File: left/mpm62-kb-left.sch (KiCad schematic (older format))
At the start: 65 parts, among them J1 Conn_01x04_Male, SW1 SW_Push, U1 ProMicro

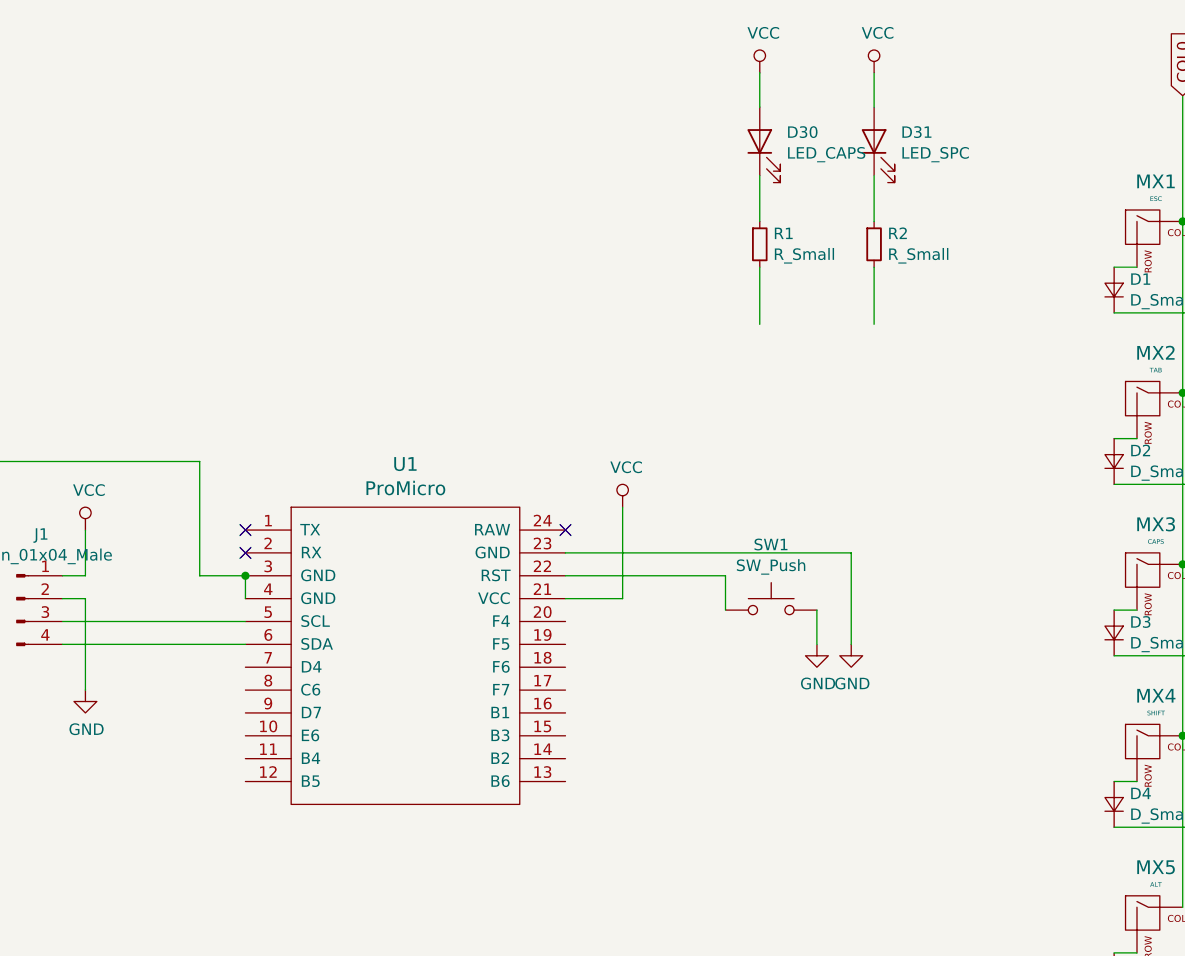
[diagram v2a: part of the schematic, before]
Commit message: Left side routed.
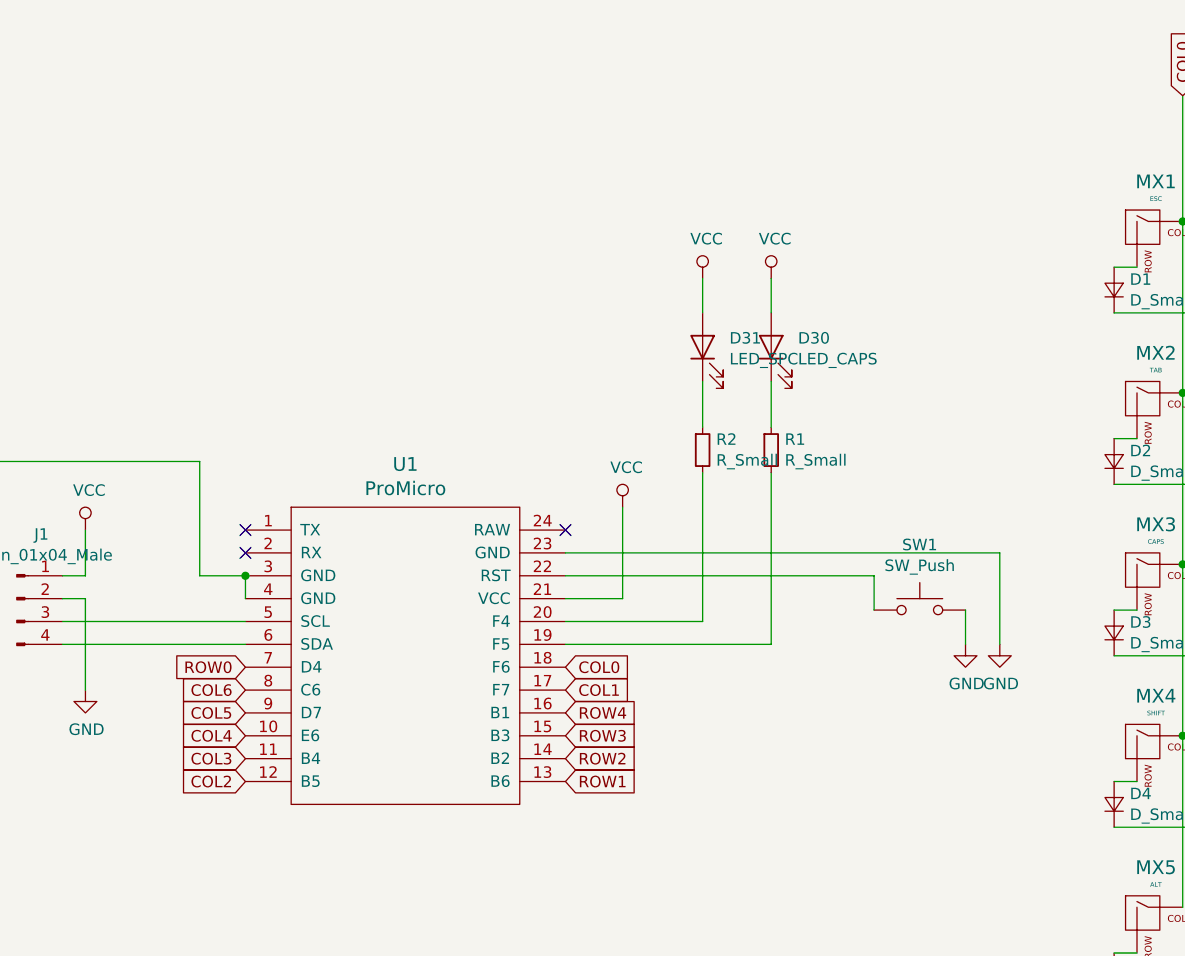
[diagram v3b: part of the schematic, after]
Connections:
- net COL0: now also U1.18 (F6)
- net COL1: now also U1.17 (F7)
- net COL2: now also U1.12 (B5)
- net COL3: now also U1.11 (B4)
- net COL4: now also U1.10 (E6)
- net COL5: now also U1.9 (D7)
- net COL6: now also U1.8 (C6)
- net ROW0: now also U1.7 (D4)
- net ROW1: now also U1.13 (B6)
- net ROW2: now also U1.14 (B2)
- net ROW3: now also U1.15 (B3)
- net ROW4: now also U1.16 (B1)
- net at U1.19 (F5): now also R1.2
- net at U1.20 (F4): now also R2.2
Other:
- moved on the sheet: D30, D31, R1, R2, SW1
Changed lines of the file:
@@
 L Device:R_Small R1
 U 1 1 5F89BC79
-P 4800 2150
-F 0 "R1" H 4859 2196 50  0000 L CNN
-F 1 "R_Small" H 4859 2105 50  0000 L CNN
-F 2 "Resistor_THT:R_Axial_DIN0204_L3.6mm_D1.6mm_P5.08mm_Horizontal" H 4800 2150 50  0001 C CNN
-F 3 "~" H 4800 2150 50  0001 C CNN
-	1    4800 2150
-	1    0    0    -1
-$EndComp
-Wire Wire Line
-	4800 1400 4800 1550
+P 4850 3050
+F 0 "R1" H 4909 3096 50  0000 L CNN
+F 1 "R_Small" H 4909 3005 50  0000 L CNN
+F 2 "Resistor_THT:R_Axial_DIN0204_L3.6mm_D1.6mm_P5.08mm_Horizontal" H 4850 3050 50  0001 C CNN
+F 3 "~" H 4850 3050 50  0001 C CNN
+	1    4850 3050
+	1    0    0    -1
+$EndComp
+Wire Wire Line
+	4850 2300 4850 2450
 $Comp
 L Device:LED D30
 U 1 1 5F893C40
-P 4800 1700
-F 0 "D30" V 4839 1583 50  0000 R CNN
-F 1 "LED_CAPS" V 4748 1583 50  0000 R CNN
-F 2 "LED_THT:LED_D3.0mm" H 4800 1700 50  0001 C CNN
-F 3 "~" H 4800 1700 50  0001 C CNN
-	1    4800 1700
+P 4850 2600
+F 0 "D30" V 4889 2483 50  0000 R CNN
+F 1 "LED_CAPS" V 4798 2483 50  0000 R CNN
+F 2 "LED_THT:LED_D3.0mm" H 4850 2600 50  0001 C CNN
+F 3 "~" H 4850 2600 50  0001 C CNN
+	1    4850 2600
 	0    -1   -1   0
 $EndComp
 Wire Wire Line
-	4800 1850 4800 2050
-Wire Wire Line
-	4800 2250 4800 2500
+	4850 2750 4850 2950
 $Comp
 L Device:R_Small R2
 U 1 1 5F8B9477
-P 5300 2150
-F 0 "R2" H 5359 2196 50  0000 L CNN
-F 1 "R_Small" H 5359 2105 50  0000 L CNN
-F 2 "Resistor_THT:R_Axial_DIN0204_L3.6mm_D1.6mm_P5.08mm_Horizontal" H 5300 2150 50  0001 C CNN
-F 3 "~" H 5300 2150 50  0001 C CNN
-	1    5300 2150
-	1    0    0    -1
-$EndComp
-Wire Wire Line
-	5300 1400 5300 1550
+P 4550 3050
+F 0 "R2" H 4609 3096 50  0000 L CNN
+F 1 "R_Small" H 4609 3005 50  0000 L CNN
+F 2 "Resistor_THT:R_Axial_DIN0204_L3.6mm_D1.6mm_P5.08mm_Horizontal" H 4550 3050 50  0001 C CNN
+F 3 "~" H 4550 3050 50  0001 C CNN
+	1    4550 3050
+	1    0    0    -1
+$EndComp
+Wire Wire Line
+	4550 2300 4550 2450
 $Comp
 L Device:LED D31
 U 1 1 5F8B947E
-P 5300 1700
-F 0 "D31" V 5339 1583 50  0000 R CNN
-F 1 "LED_SPC " V 5248 1583 50  0000 R CNN
-F 2 "LED_THT:LED_D3.0mm" H 5300 1700 50  0001 C CNN
-F 3 "~" H 5300 1700 50  0001 C CNN
-	1    5300 1700
+P 4550 2600
+F 0 "D31" V 4589 2483 50  0000 R CNN
+F 1 "LED_SPC " V 4498 2483 50  0000 R CNN
+F 2 "LED_THT:LED_D3.0mm" H 4550 2600 50  0001 C CNN
+F 3 "~" H 4550 2600 50  0001 C CNN
+	1    4550 2600
 	0    -1   -1   0
 $EndComp
 Wire Wire Line
-	5300 1850 5300 2050
-Wire Wire Line
-	5300 2250 5300 2500
+	4550 2750 4550 2950
 $Comp
 L promicro:ProMicro U1
@@
 L power:GND #PWR0102
 U 1 1 5F790069
-P 5200 3900
-F 0 "#PWR0102" H 5200 3650 50  0001 C CNN
-F 1 "GND" H 5205 3727 50  0000 C CNN
-F 2 "" H 5200 3900 50  0001 C CNN
-F 3 "" H 5200 3900 50  0001 C CNN
-	1    5200 3900
-	1    0    0    -1
-$EndComp
-Wire Wire Line
-	5200 3500 3950 3500
+P 5850 3900
+F 0 "#PWR0102" H 5850 3650 50  0001 C CNN
+F 1 "GND" H 5855 3727 50  0000 C CNN
+F 2 "" H 5850 3900 50  0001 C CNN
+F 3 "" H 5850 3900 50  0001 C CNN
+	1    5850 3900
+	1    0    0    -1
+$EndComp
 $Comp
 L Switch:SW_Push SW1
 U 1 1 5F7953DA
-P 4850 3750
-F 0 "SW1" H 4850 4035 50  0000 C CNN
-F 1 "SW_Push" H 4850 3944 50  0000 C CNN
-F 2 "random-keyboard-parts:SKQG-1155865" H 4850 3950 50  0001 C CNN
-F 3 "~" H 4850 3950 50  0001 C CNN
-	1    4850 3750
-	1    0    0    -1
-$EndComp
-Wire Wire Line
-	3950 3600 4650 3600
-Wire Wire Line
-	4650 3600 4650 3750
+P 5500 3750
+F 0 "SW1" H 5500 4035 50  0000 C CNN
+F 1 "SW_Push" H 5500 3944 50  0000 C CNN
+F 2 "random-keyboard-parts:SKQG-1155865" H 5500 3950 50  0001 C CNN
+F 3 "~" H 5500 3950 50  0001 C CNN
+	1    5500 3750
+	1    0    0    -1
+$EndComp
+Wire Wire Line
+	5300 3600 5300 3750
 $Comp
 L power:GND #PWR0103
 U 1 1 5F79987A
-P 5050 3900
-F 0 "#PWR0103" H 5050 3650 50  0001 C CNN
-F 1 "GND" H 5055 3727 50  0000 C CNN
-F 2 "" H 5050 3900 50  0001 C CNN
-F 3 "" H 5050 3900 50  0001 C CNN
-	1    5050 3900
-	1    0    0    -1
-$EndComp
-Wire Wire Line
-	5050 3750 5050 3900
-Wire Wire Line
-	5200 3500 5200 3900
+P 5700 3900
+F 0 "#PWR0103" H 5700 3650 50  0001 C CNN
+F 1 "GND" H 5705 3727 50  0000 C CNN
+F 2 "" H 5700 3900 50  0001 C CNN
+F 3 "" H 5700 3900 50  0001 C CNN
+	1    5700 3900
+	1    0    0    -1
+$EndComp
+Wire Wire Line
+	5700 3750 5700 3900
+Wire Wire Line
+	5850 3500 5850 3900
 $Comp
 L Connector:Conn_01x04_Male J1
@@
 L power:VCC #PWR0107
 U 1 1 5F7BD1F6
-P 4800 1400
-F 0 "#PWR0107" H 4800 1250 50  0001 C CNN
-F 1 "VCC" H 4817 1573 50  0000 C CNN
-F 2 "" H 4800 1400 50  0001 C CNN
-F 3 "" H 4800 1400 50  0001 C CNN
-	1    4800 1400
+P 4850 2300
+F 0 "#PWR0107" H 4850 2150 50  0001 C CNN
+F 1 "VCC" H 4867 2473 50  0000 C CNN
+F 2 "" H 4850 2300 50  0001 C CNN
+F 3 "" H 4850 2300 50  0001 C CNN
+	1    4850 2300
 	1    0    0    -1
 $EndComp
@@
 L power:VCC #PWR0108
 U 1 1 5F7BD887
-P 5300 1400
-F 0 "#PWR0108" H 5300 1250 50  0001 C CNN
-F 1 "VCC" H 5317 1573 50  0000 C CNN
-F 2 "" H 5300 1400 50  0001 C CNN
-F 3 "" H 5300 1400 50  0001 C CNN
-	1    5300 1400
+P 4550 2300
+F 0 "#PWR0108" H 4550 2150 50  0001 C CNN
+F 1 "VCC" H 4567 2473 50  0000 C CNN
+F 2 "" H 4550 2300 50  0001 C CNN
+F 3 "" H 4550 2300 50  0001 C CNN
+	1    4550 2300
 	1    0    0    -1
 $EndComp
@@
 	8650 4300 8650 5050
 Connection ~ 8650 4300
+Text GLabel 2550 4300 0    50   Input ~ 0
+COL4
+Text GLabel 2550 4000 0    50   Input ~ 0
+ROW0
+Text GLabel 3950 4000 2    50   Input ~ 0
+COL0
+Text GLabel 3950 4100 2    50   Input ~ 0
+COL1
+Text GLabel 3950 4500 2    50   Input ~ 0
+ROW1
+Text GLabel 3950 4400 2    50   Input ~ 0
+ROW2
+Text GLabel 3950 4300 2    50   Input ~ 0
+ROW3
+Text GLabel 3950 4200 2    50   Input ~ 0
+ROW4
+Wire Wire Line
+	3950 3500 5850 3500
+Wire Wire Line
+	3950 3600 5300 3600
+Text GLabel 2550 4100 0    50   Input ~ 0
+COL6
+Text GLabel 2550 4200 0    50   Input ~ 0
+COL5
+Text GLabel 2550 4400 0    50   Input ~ 0
+COL3
+Text GLabel 2550 4500 0    50   Input ~ 0
+COL2
+Wire Wire Line
+	4550 3150 4550 3800
+Wire Wire Line
+	4550 3800 3950 3800
+Wire Wire Line
+	4850 3900 3950 3900
+Wire Wire Line
+	4850 3150 4850 3900
 $EndSCHEMATC

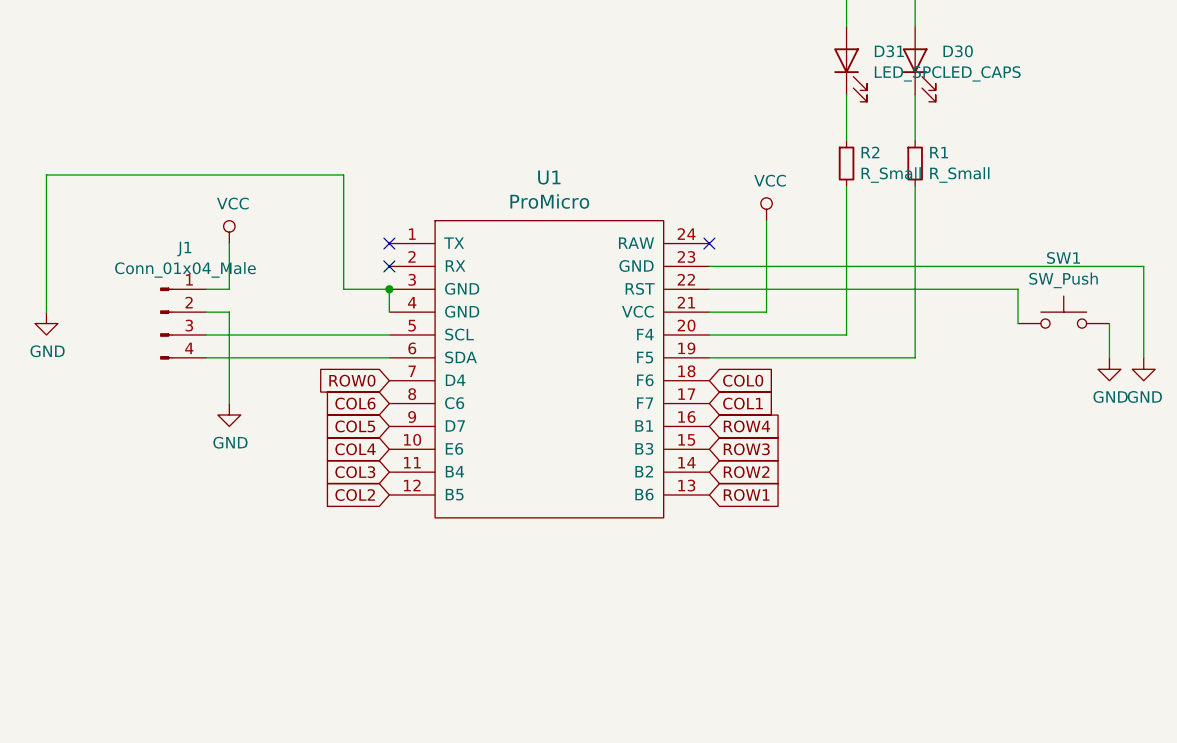
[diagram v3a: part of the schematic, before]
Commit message: Fix issues with left side: 1. SCL and SDA are swapped in the library file from github/ProMicroKiCad. Current fix is to swap the wires and mark the schematic to show which is which. Ultimately it would be good to get an updated lib file, but there is a PR for this which has never been accepted. 2. Was missing pullup resistors for I2C bus. 3. Resistor sizes on PCB were smaller than typical TH resistors. 4. Added extra header for power and ground to ease debugging.
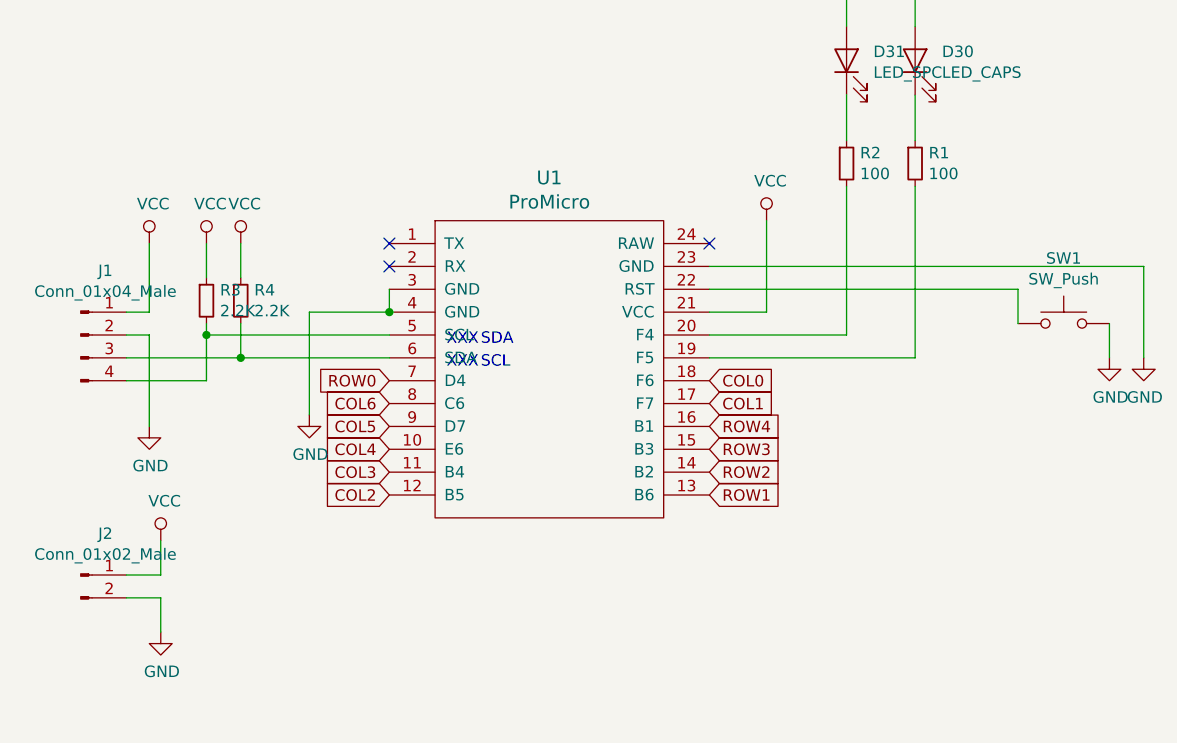
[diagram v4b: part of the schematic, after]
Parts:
- added J2: Conn_01x02_Male, Connector_PinHeader_2.54mm:PinHeader_1x02_P2.54mm_Vertical, symbol Connector:Conn_01x02_Male
- added R3, R4: 2.2K, Resistor_THT:R_Axial_DIN0207_L6.3mm_D2.5mm_P7.62mm_Horizontal, symbol Device:R_Small
- MX23: footprint MX_Alps_Hybrid:MX-3U-NoLED -> MX_Alps_Hybrid:MX-3U-ReversedStabilizers-NoLED
- R1, R2: value R_Small -> 100; footprint Resistor_THT:R_Axial_DIN0204_L3.6mm_D1.6mm_P5.08mm_Horizontal -> Resistor_THT:R_Axial_DIN0207_L6.3mm_D2.5mm_P7.62mm_Horizontal
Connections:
- net GND: now also J2.2 (Pin_2)
- net VCC: now also J2.1 (Pin_1), R3.1, R4.1
- net at U1.5 (SCL): now also J1.4 (Pin_4), R3.2; no longer J1.3 (Pin_3)
- net at U1.6 (SDA): now also J1.3 (Pin_3), R4.2; no longer J1.4 (Pin_4)
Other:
- note added: "SCL"
- note added: "SDA"
- note added: "XXX"
- moved on the sheet: J1
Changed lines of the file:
@@
 F 0 "MX23" H 8533 5323 60  0000 C CNN
 F 1 "SPC" H 8533 5249 20  0000 C CNN
-F 2 "MX_Alps_Hybrid:MX-3U-NoLED" H 7875 5075 60  0001 C CNN
+F 2 "MX_Alps_Hybrid:MX-3U-ReversedStabilizers-NoLED" H 7875 5075 60  0001 C CNN
 F 3 "" H 7875 5075 60  0001 C CNN
 	1    8500 5100
@@
 P 4850 3050
 F 0 "R1" H 4909 3096 50  0000 L CNN
-F 1 "R_Small" H 4909 3005 50  0000 L CNN
-F 2 "Resistor_THT:R_Axial_DIN0204_L3.6mm_D1.6mm_P5.08mm_Horizontal" H 4850 3050 50  0001 C CNN
+F 1 "100" H 4909 3005 50  0000 L CNN
+F 2 "Resistor_THT:R_Axial_DIN0207_L6.3mm_D2.5mm_P7.62mm_Horizontal" H 4850 3050 50  0001 C CNN
 F 3 "~" H 4850 3050 50  0001 C CNN
 	1    4850 3050
@@
 P 4550 3050
 F 0 "R2" H 4609 3096 50  0000 L CNN
-F 1 "R_Small" H 4609 3005 50  0000 L CNN
-F 2 "Resistor_THT:R_Axial_DIN0204_L3.6mm_D1.6mm_P5.08mm_Horizontal" H 4550 3050 50  0001 C CNN
+F 1 "100" H 4609 3005 50  0000 L CNN
+F 2 "Resistor_THT:R_Axial_DIN0207_L6.3mm_D2.5mm_P7.62mm_Horizontal" H 4550 3050 50  0001 C CNN
 F 3 "~" H 4550 3050 50  0001 C CNN
 	1    4550 3050
@@
 L power:GND #PWR0101
 U 1 1 5F7863E5
-P 1050 3700
-F 0 "#PWR0101" H 1050 3450 50  0001 C CNN
-F 1 "GND" H 1055 3527 50  0000 C CNN
-F 2 "" H 1050 3700 50  0001 C CNN
-F 3 "" H 1050 3700 50  0001 C CNN
-	1    1050 3700
+P 2200 4150
+F 0 "#PWR0101" H 2200 3900 50  0001 C CNN
+F 1 "GND" H 2205 3977 50  0000 C CNN
+F 2 "" H 2200 4150 50  0001 C CNN
+F 3 "" H 2200 4150 50  0001 C CNN
+	1    2200 4150
 	1    0    0    -1
 $EndComp
@@
 L Connector:Conn_01x04_Male J1
 U 1 1 5F7A1803
-P 1550 3700
-F 0 "J1" H 1658 3981 50  0000 C CNN
-F 1 "Conn_01x04_Male" H 1658 3890 50  0000 C CNN
-F 2 "Connector_PinHeader_2.54mm:PinHeader_1x04_P2.54mm_Vertical" H 1550 3700 50  0001 C CNN
-F 3 "~" H 1550 3700 50  0001 C CNN
-	1    1550 3700
-	1    0    0    -1
-$EndComp
-Wire Wire Line
-	2550 3600 2350 3600
-Wire Wire Line
-	2350 3600 2350 3100
-Wire Wire Line
-	2350 3100 1050 3100
-Wire Wire Line
-	1050 3100 1050 3700
-Connection ~ 2550 3600
-Wire Wire Line
-	2550 3800 1750 3800
-Wire Wire Line
-	2550 3900 1750 3900
+P 1200 3800
+F 0 "J1" H 1308 4081 50  0000 C CNN
+F 1 "Conn_01x04_Male" H 1308 3990 50  0000 C CNN
+F 2 "Connector_PinHeader_2.54mm:PinHeader_1x04_P2.54mm_Vertical" H 1200 3800 50  0001 C CNN
+F 3 "~" H 1200 3800 50  0001 C CNN
+	1    1200 3800
+	1    0    0    -1
+$EndComp
 $Comp
 L power:GND #PWR0104
 U 1 1 5F7AF8D5
-P 1850 4100
-F 0 "#PWR0104" H 1850 3850 50  0001 C CNN
-F 1 "GND" H 1855 3927 50  0000 C CNN
-F 2 "" H 1850 4100 50  0001 C CNN
-F 3 "" H 1850 4100 50  0001 C CNN
-	1    1850 4100
-	1    0    0    -1
-$EndComp
-Wire Wire Line
-	1750 3700 1850 3700
-Wire Wire Line
-	1850 3700 1850 4100
-$Comp
-L power:VCC #PWR0105
-U 1 1 5F7B3E75
-P 1850 3400
-F 0 "#PWR0105" H 1850 3250 50  0001 C CNN
-F 1 "VCC" H 1867 3573 50  0000 C CNN
-F 2 "" H 1850 3400 50  0001 C CNN
-F 3 "" H 1850 3400 50  0001 C CNN
-	1    1850 3400
-	1    0    0    -1
-$EndComp
-Wire Wire Line
-	1750 3600 1850 3600
-Wire Wire Line
-	1850 3600 1850 3400
+P 1500 4200
+F 0 "#PWR0104" H 1500 3950 50  0001 C CNN
+F 1 "GND" H 1505 4027 50  0000 C CNN
+F 2 "" H 1500 4200 50  0001 C CNN
+F 3 "" H 1500 4200 50  0001 C CNN
+	1    1500 4200
+	1    0    0    -1
+$EndComp
+Wire Wire Line
+	1400 3800 1500 3800
+Wire Wire Line
+	1500 3800 1500 4200
+Wire Wire Line
+	1400 3700 1500 3700
 Wire Wire Line
 	3950 3700 4200 3700
@@
 Wire Wire Line
 	4850 3150 4850 3900
+$Comp
+L Device:R_Small R3
+U 1 1 5F98F436
+P 1750 3650
+F 0 "R3" H 1809 3696 50  0000 L CNN
+F 1 "2.2K" H 1809 3605 50  0000 L CNN
+F 2 "Resistor_THT:R_Axial_DIN0207_L6.3mm_D2.5mm_P7.62mm_Horizontal" H 1750 3650 50  0001 C CNN
+F 3 "~" H 1750 3650 50  0001 C CNN
+	1    1750 3650
+	1    0    0    -1
+$EndComp
+$Comp
+L Device:R_Small R4
+U 1 1 5F98FEB2
+P 1900 3650
+F 0 "R4" H 1959 3696 50  0000 L CNN
+F 1 "2.2K" H 1959 3605 50  0000 L CNN
+F 2 "Resistor_THT:R_Axial_DIN0207_L6.3mm_D2.5mm_P7.62mm_Horizontal" H 1900 3650 50  0001 C CNN
+F 3 "~" H 1900 3650 50  0001 C CNN
+	1    1900 3650
+	1    0    0    -1
+$EndComp
+$Comp
+L power:VCC #PWR0105
+U 1 1 5F7B3E75
+P 1500 3400
+F 0 "#PWR0105" H 1500 3250 50  0001 C CNN
+F 1 "VCC" H 1517 3573 50  0000 C CNN
+F 2 "" H 1500 3400 50  0001 C CNN
+F 3 "" H 1500 3400 50  0001 C CNN
+	1    1500 3400
+	1    0    0    -1
+$EndComp
+$Comp
+L power:VCC #PWR03
+U 1 1 5F99C05C
+P 1750 3400
+F 0 "#PWR03" H 1750 3250 50  0001 C CNN
+F 1 "VCC" H 1767 3573 50  0000 C CNN
+F 2 "" H 1750 3400 50  0001 C CNN
+F 3 "" H 1750 3400 50  0001 C CNN
+	1    1750 3400
+	1    0    0    -1
+$EndComp
+$Comp
+L power:VCC #PWR04
+U 1 1 5F99FE1C
+P 1900 3400
+F 0 "#PWR04" H 1900 3250 50  0001 C CNN
+F 1 "VCC" H 1917 3573 50  0000 C CNN
+F 2 "" H 1900 3400 50  0001 C CNN
+F 3 "" H 1900 3400 50  0001 C CNN
+	1    1900 3400
+	1    0    0    -1
+$EndComp
+Wire Wire Line
+	1750 3400 1750 3550
+Wire Wire Line
+	1900 3400 1900 3550
+Wire Wire Line
+	1750 3750 1750 3800
+Wire Wire Line
+	1900 3750 1900 3900
+Wire Wire Line
+	2550 3700 2200 3700
+Wire Wire Line
+	2200 3700 2200 4150
+Connection ~ 2550 3700
+Wire Wire Line
+	1750 3800 2550 3800
+Wire Wire Line
+	1900 3900 2550 3900
+Wire Wire Line
+	1500 3700 1500 3400
+Wire Wire Line
+	1400 3900 1900 3900
+Connection ~ 1900 3900
+Wire Wire Line
+	1750 3800 1750 4000
+Wire Wire Line
+	1750 4000 1400 4000
+Connection ~ 1750 3800
+Text Notes 2950 3950 0    50   ~ 0
+SCL
+Text Notes 2950 3850 0    50   ~ 0
+SDA
+Text Notes 2800 3850 0    50   ~ 0
+XXX
+Text Notes 2800 3950 0    50   ~ 0
+XXX
+$Comp
+L Connector:Conn_01x02_Male J2
+U 1 1 5FA00E00
+P 1200 4850
+F 0 "J2" H 1308 5031 50  0000 C CNN
+F 1 "Conn_01x02_Male" H 1308 4940 50  0000 C CNN
+F 2 "Connector_PinHeader_2.54mm:PinHeader_1x02_P2.54mm_Vertical" H 1200 4850 50  0001 C CNN
+F 3 "~" H 1200 4850 50  0001 C CNN
+	1    1200 4850
+	1    0    0    -1
+$EndComp
+$Comp
+L power:VCC #PWR01
+U 1 1 5FA019D0
+P 1550 4700
+F 0 "#PWR01" H 1550 4550 50  0001 C CNN
+F 1 "VCC" H 1567 4873 50  0000 C CNN
+F 2 "" H 1550 4700 50  0001 C CNN
+F 3 "" H 1550 4700 50  0001 C CNN
+	1    1550 4700
+	1    0    0    -1
+$EndComp
+Wire Wire Line
+	1550 4700 1550 4850
+Wire Wire Line
+	1550 4850 1400 4850
+$Comp
+L power:GND #PWR02
+U 1 1 5FA0AC95
+P 1550 5100
+F 0 "#PWR02" H 1550 4850 50  0001 C CNN
+F 1 "GND" H 1555 4927 50  0000 C CNN
+F 2 "" H 1550 5100 50  0001 C CNN
+F 3 "" H 1550 5100 50  0001 C CNN
+	1    1550 5100
+	1    0    0    -1
+$EndComp
+Wire Wire Line
+	1400 4950 1550 4950
+Wire Wire Line
+	1550 4950 1550 5100
 $EndSCHEMATC
